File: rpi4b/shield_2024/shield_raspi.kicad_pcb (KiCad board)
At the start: 2 copper layers, 66 x 58 mm, 26 parts, among them J4 Conn_02x20_Odd_Even, U1 IRLML2402

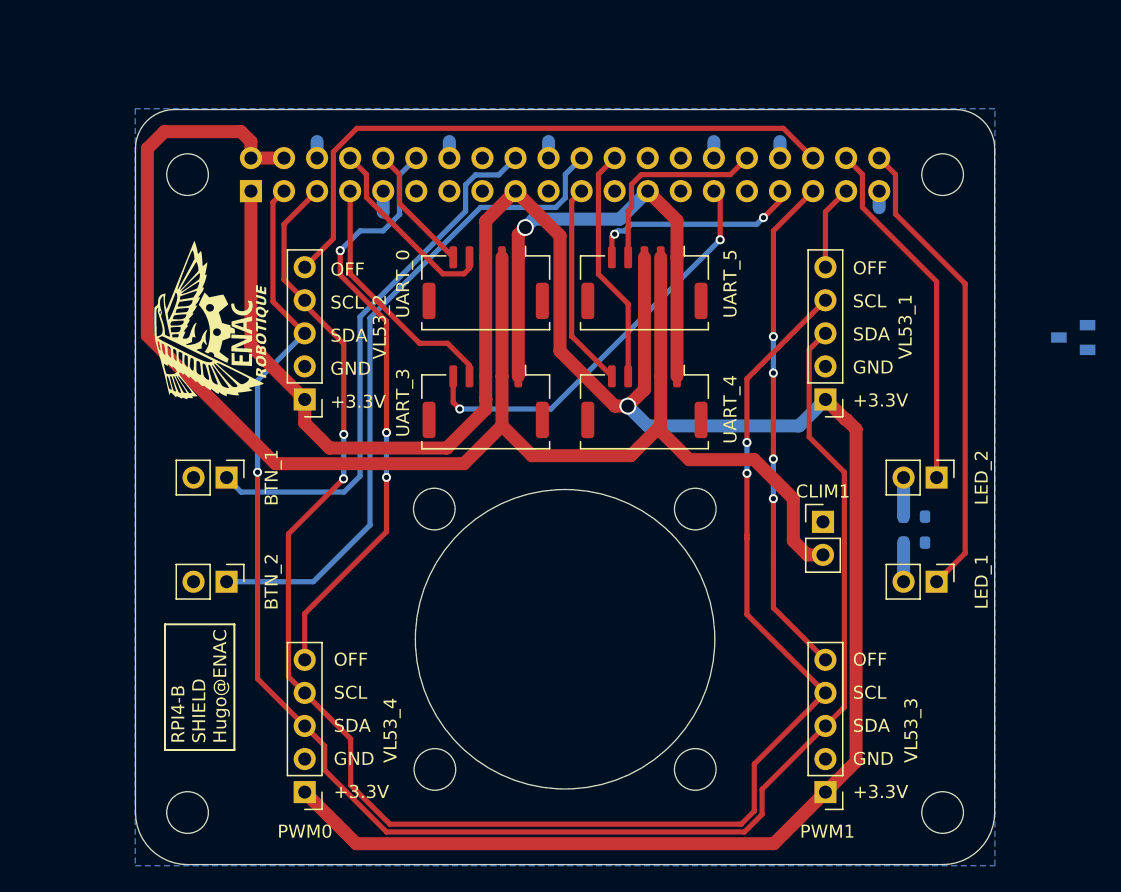
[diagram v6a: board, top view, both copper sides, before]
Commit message: ajout clim , attente de validation
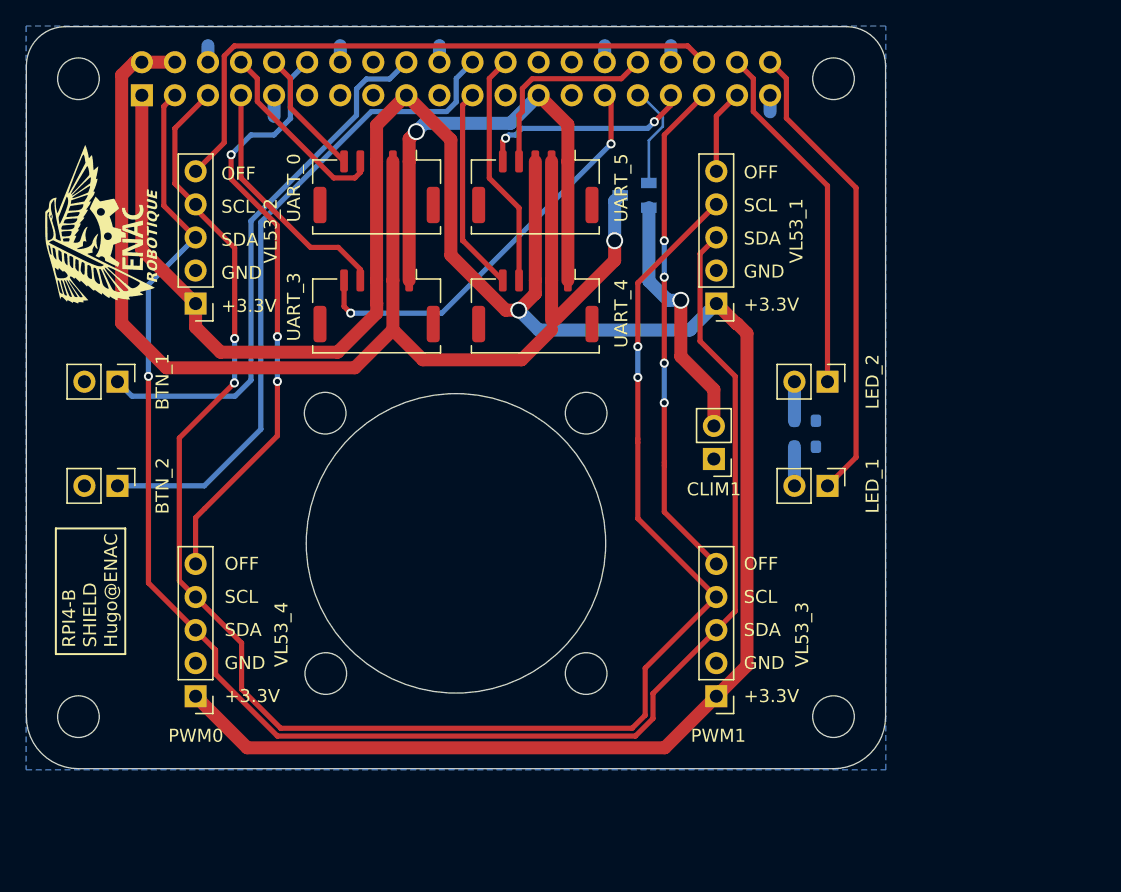
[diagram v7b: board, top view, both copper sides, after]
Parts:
- moved U1 35.4 mm to (177.8, 87.7)
- moved VL53_3 11.2 mm to (184.1, 126.2)
- moved VL53_4 11.2 mm to (144.1, 126.2)
- moved BTN_1 11.2 mm to (138.1, 102.0)
- moved BTN_2 11.2 mm to (138.1, 110.0)
- moved G*** 11.2 mm to (136.5, 90.9)
- moved H1 11.2 mm to (135.1, 78.7)
- moved H2 11.2 mm to (193.1, 78.7)
- moved H3 11.2 mm to (193.1, 127.7)
- moved H4 11.2 mm to (135.1, 127.7)
- moved H6 11.2 mm to (174.1, 104.4)
- moved J4 11.2 mm to (140.0, 80.0)
- moved LED_1 11.2 mm to (192.6, 110.0)
- moved LED_2 11.2 mm to (192.6, 102.0)
- moved R1 11.2 mm to (190.9, 107.0)
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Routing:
- net +5V: track 118.2 -> 97.9 mm, vias 0 -> 1
- net Net-(CLIM1-Pin_2): track 0.00 -> 19.4 mm, vias 0 -> 1
- net CLIM: track 0.00 -> 8.12 mm
- net VL53_2: track 48.3 -> 47.5 mm
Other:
- board size 66 x 58 mm -> 66 x 57 mm

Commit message: trou caméra
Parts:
- moved H7 34.7 mm to (182.5, 104.6)
- moved UART_0 34.7 mm to (186.4, 67.2)
- moved BTN_1 34.7 mm to (166.5, 82.2)
- moved BTN_2 34.7 mm to (166.5, 90.2)
- moved CLIM1 34.7 mm to (212.3, 88.1)
- moved H1 34.7 mm to (163.5, 58.9)
- moved H2 34.7 mm to (221.5, 58.9)
- moved H3 34.7 mm to (221.5, 107.9)
- moved H4 34.7 mm to (163.5, 107.9)
- moved LED_1 34.7 mm to (221.1, 90.2)
- moved LED_2 34.7 mm to (221.1, 82.2)
- moved R1 34.7 mm to (219.4, 87.2)
- moved R2 34.7 mm to (219.4, 85.2)
- moved UART_3 34.7 mm to (186.4, 76.4)
- moved VL53_1 34.7 mm to (212.5, 76.2)
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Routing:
- net SCL: track 131.5 -> 110.1 mm, vias 4 -> 2
- net SDA: track 126.8 -> 141.0 mm, vias 1 -> 4
- net BTN_2: track 51.1 -> 49.0 mm
- net +3.3V: track 177.9 -> 178.7 mm, vias 1 -> 2
- net +5V: track 97.9 -> 98.7 mm
- net CLIM: track 8.12 -> 7.34 mm
- net VL53_3: vias 4 -> 2
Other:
- outline, holes or cut-outs redrawn
- board text added: "JLCJLCJLCJLC"
